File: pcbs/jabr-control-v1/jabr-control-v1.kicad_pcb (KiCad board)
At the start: 6 copper layers, 70 x 80 mm, 245 parts, among them J10001 ARJM11D7-502-AB-EW2, J10002 TYPE-C-31-M-12, J1001 48406-0003, J201 JST-SH-4-Vertical, J4001 MDT320E0X001, J401 U.FL-R-SMT-K_895, J402 U.FL-R-SMT-K_895, J6001 MSPE-J2L0-x00, J9001 43045-0201, Q2602 DMN21D2UFB-7B, SW202 TS20-42-25-WT-160-SMT-TR, U1001 AP22653FDZ-7, U1002 PESD4USB3BTTS-QX, U1003 PESD4USB3BTTS-QX, U1004 PESD4USB3BTTS-QX, U1005 PESD4USB3BTTS-QX, U1201 TPS259472ARPWR, U1301 MAX20004AFOC/VY+T, U1401 TPS62290TDRVRQ1, U1501 TPS62290TDRVRQ1, U201 NX3DV221TKX, U2401 PESD4USB3BTTS-QX, U2402 PESD4USB3BTTS-QX, U301 TVS3301DRBR, U302 TPS26600RHFR, U303 PI7C9X2G304SL, U3801 TPS62290TDRVRQ1, U401 LMQ66430MC3RXBRQ1, U402 TPS7B8133QDRVRQ1, U403 TPS2116DRL, U5001 LAN7431_YXX, U8001 LAN8870, Y401 ASEK-32.768KHZ-LRT, Y8001 XRCGB25M000F3A16R0

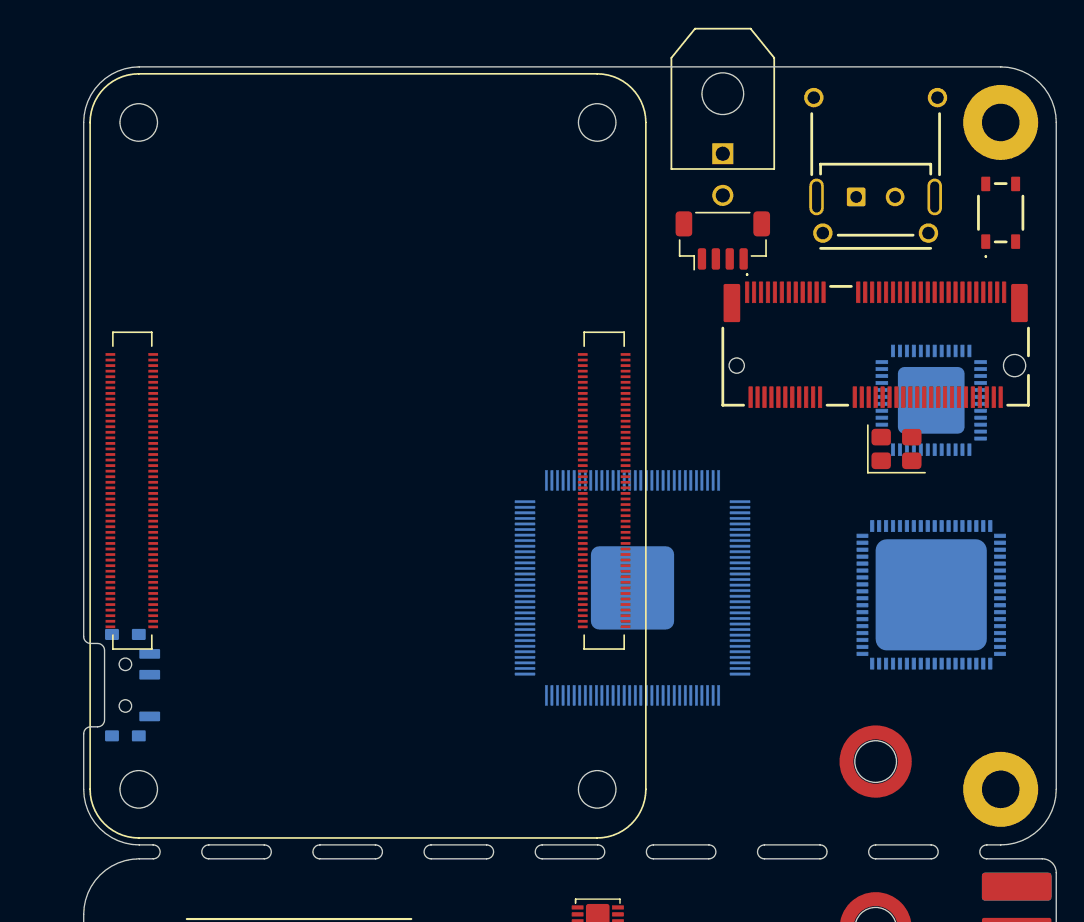
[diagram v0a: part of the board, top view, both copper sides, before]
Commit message: Updated FH12-22S-0.5SH footprints
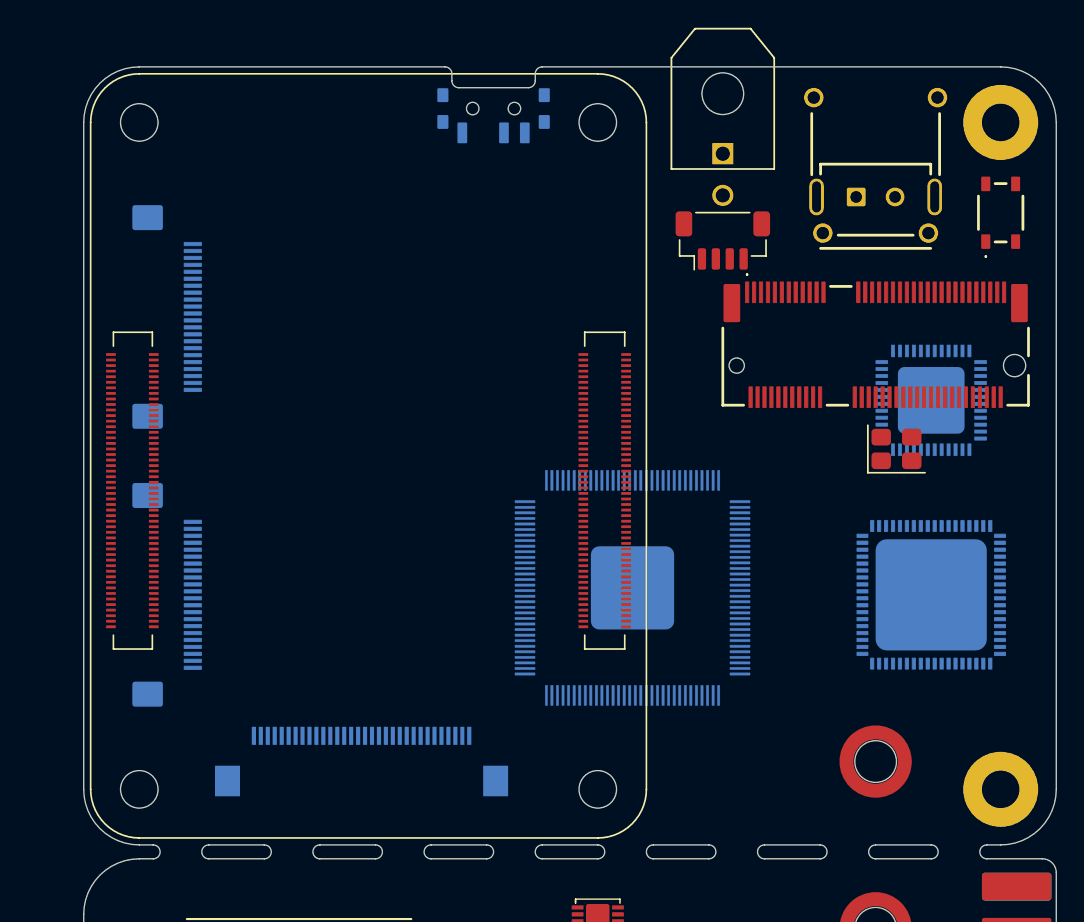
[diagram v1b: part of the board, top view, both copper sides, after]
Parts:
- added J1501: FH12-22S-0.5SH, project_footprints:Hirose_FH12-22S-0.5SH_1x22-1MP_P0.50mm_Horizontal, B.Cu at (135.0, 81.0)
- added J1502: FH12-22S-0.5SH, project_footprints:Hirose_FH12-22S-0.5SH_1x22-1MP_P0.50mm_Horizontal, B.Cu at (135.0, 101.0)
- added REF**: Hirose_FH12-32S-0.5SH_1x32-1MP_P0.50mm_Horizontal, Connector_FFC-FPC:Hirose_FH12-32S-0.5SH_1x32-1MP_P0.50mm_Horizontal, B.Cu at (149.0, 113.0)
- moved S201 49.2 mm to (158.5, 66.0), turned to 0 degrees
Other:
- outline, holes or cut-outs redrawn

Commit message: Added v2 project
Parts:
- removed AE401, AE402: EMPCB.SMAFSTJ.B.HT, project_footprints:sma_edge_mount
- removed J401, J402: U.FL-R-SMT-K_895, project_footprints:UFLRSMTK895
- removed REF**: Hirose_FH12-32S-0.5SH_1x32-1MP_P0.50mm_Horizontal, Connector_FFC-FPC:Hirose_FH12-32S-0.5SH_1x32-1MP_P0.50mm_Horizontal
- added J1002: FH12-22S-0.5SH, project_footprints:Hirose_FH12-22S-0.5SH_1x22-1MP_P0.50mm_Horizontal, F.Cu at (90.8, 150.1)
- added R306: 330R, project_footprints:R_0402, F.Cu at (98.4, 141.6)
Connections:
- U303 pad 28: unconnected-(U303B-PWR_SAV-Pad28) -> /PCIe Switch/PWR_SAV
